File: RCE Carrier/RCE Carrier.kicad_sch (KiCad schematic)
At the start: 2 parts, among them J5 DF40C-34DP-0.4V_58_, J7 DF40C-34DP-0.4V_58_

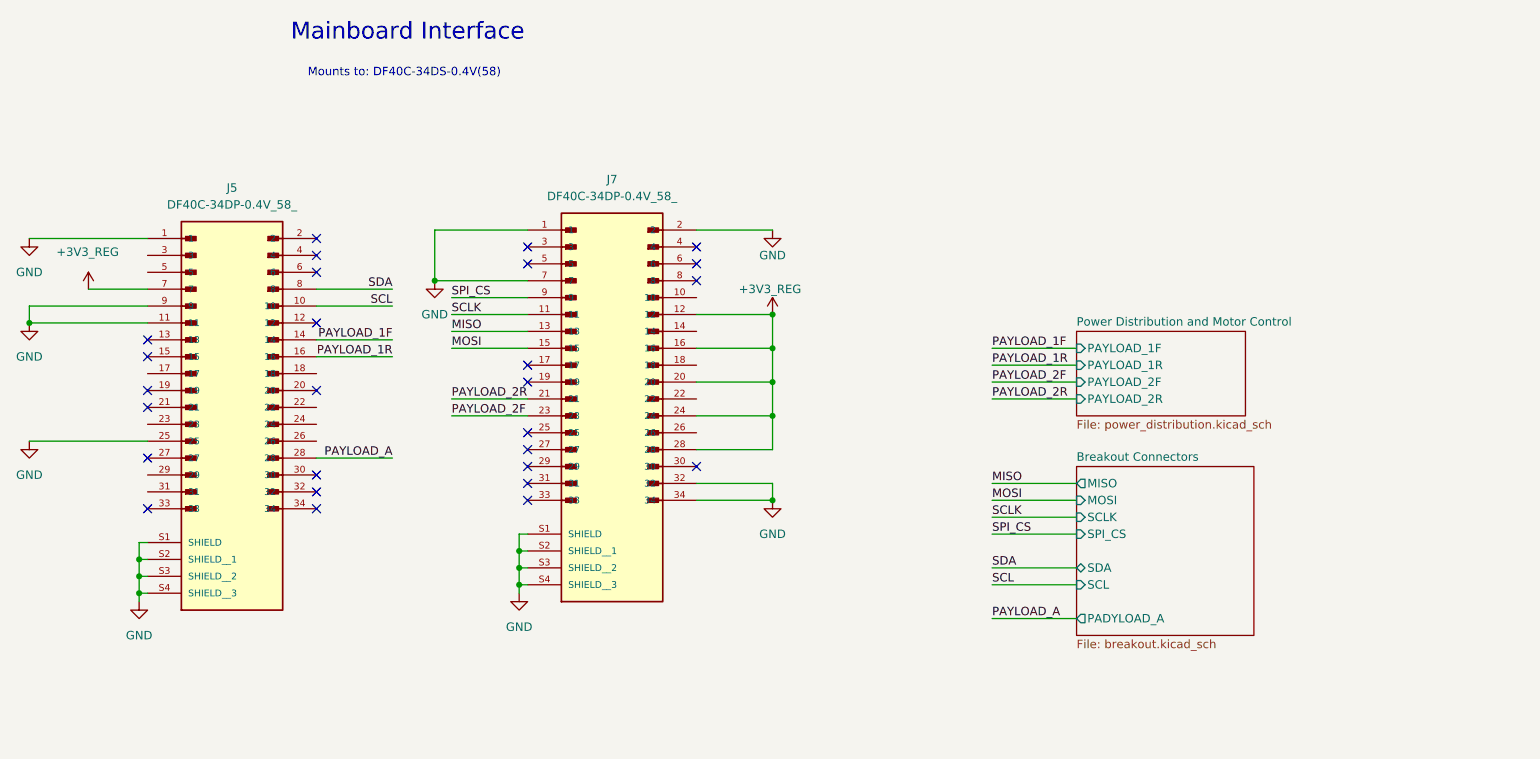
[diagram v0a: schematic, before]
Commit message: split pce and rce functions into two carriers, initial rce parts placement
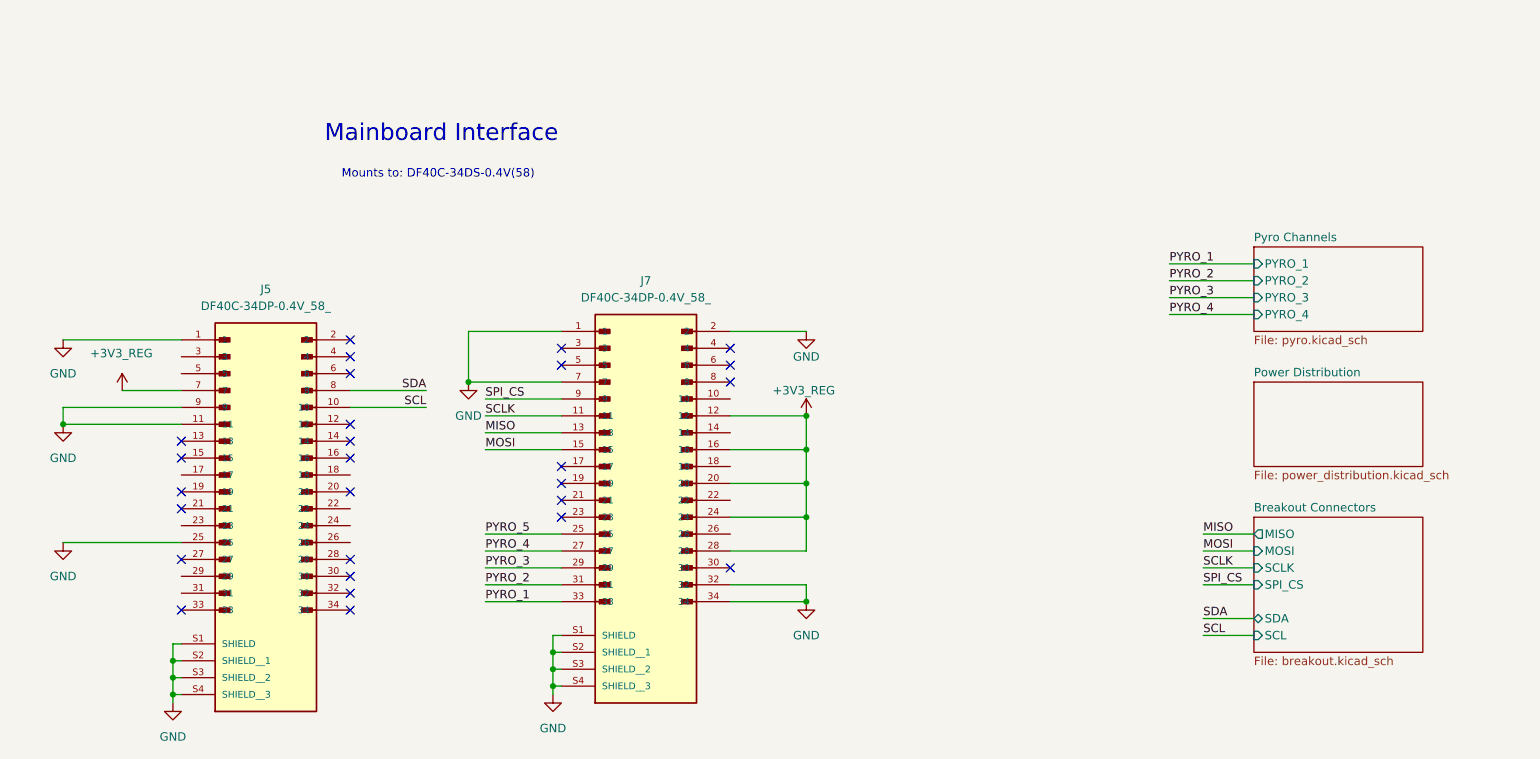
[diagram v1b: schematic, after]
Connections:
- net PYRO_5: now reaches J7.25
- net PYRO_4: now reaches J7.27
- net PYRO_3: now reaches J7.29
- net PYRO_2: now reaches J7.31
- net PYRO_1: now reaches J7.33
- net PAYLOAD_1F: no longer names the net of J5.14
- net PAYLOAD_1R: no longer names the net of J5.16
- net PAYLOAD_2F: no longer names the net of J7.23
- net PAYLOAD_2R: no longer names the net of J7.21
- net PAYLOAD_A: no longer names the net of J5.28
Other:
- removed sheet Power Distribution and Motor Control
- added sheet Power Distribution (power_distribution.kicad_sch)
- added sheet Pyro Channels (pyro.kicad_sch)
- sheet Breakout Connectors ports: added none; removed PADYLOAD_A
- title: Airdahl Flight Computer PCE Carrier Board -> Airdahl Flight Computer RCE Carrier Board

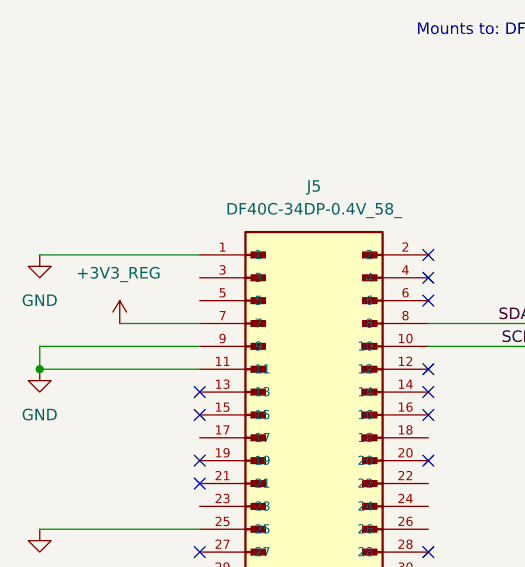
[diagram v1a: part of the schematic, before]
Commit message: added payload solenoid gpio, 3v3 rail from power mux to carriers, finished wiring
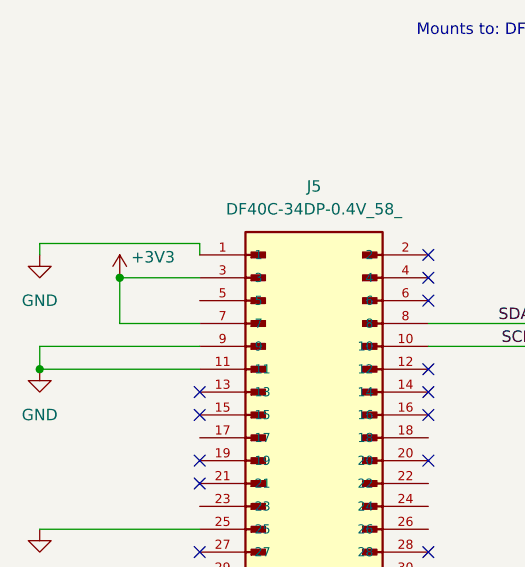
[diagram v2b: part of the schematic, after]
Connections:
- net +3V3_REG: no longer J5.7
- net +3V3: now reaches J5.3
- net +3V3: now also J5.7
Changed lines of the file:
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@@
+	)
+	(junction
+		(at 44.45 113.03)
+		(diameter 0)
+		(color 0 0 0 0)
 	)
 	(junction
@@
 	(wire
 		(pts
+			(xy 44.45 118.11) (xy 53.34 118.11)
+		)
+		(stroke
+			(width 0)
+			(type default)
+		)
+	)
+	(wire
+		(pts
 			(xy 99.06 119.38) (xy 110.49 119.38)
 		)
@@
 	(wire
 		(pts
+			(xy 53.34 109.22) (xy 53.34 110.49)
+		)
+		(stroke
+			(width 0)
+			(type default)
+		)
+	)
+	(wire
+		(pts
 			(xy 135.89 121.92) (xy 147.32 121.92)
 		)
@@
 	(wire
 		(pts
-			(xy 35.56 110.49) (xy 53.34 110.49)
+			(xy 35.56 109.22) (xy 53.34 109.22)
 		)
 		(stroke
@@
 	(wire
 		(pts
+			(xy 35.56 109.22) (xy 35.56 110.49)
+		)
+		(stroke
+			(width 0)
+			(type default)
+		)
+	)
+	(wire
+		(pts
+			(xy 44.45 113.03) (xy 53.34 113.03)
+		)
+		(stroke
+			(width 0)
+			(type default)
+		)
+	)
+	(wire
+		(pts
 			(xy 201.93 106.68) (xy 214.63 106.68)
 		)
@@
 	(wire
 		(pts
-			(xy 44.45 118.11) (xy 53.34 118.11)
-		)
-		(stroke
-			(width 0)
-			(type default)
-		)
-	)
-	(wire
-		(pts
 			(xy 52.07 165.1) (xy 52.07 163.83)
 		)
@@
 		(pts
 			(xy 78.74 118.11) (xy 90.17 118.11)
+		)
+		(stroke
+			(width 0)
+			(type default)
+		)
+	)
+	(wire
+		(pts
+			(xy 44.45 113.03) (xy 44.45 118.11)
 		)
 		(stroke
@@
 	(symbol
 		(lib_id "power:+3.3V")
-		(at 44.45 118.11 0)
+		(at 44.45 113.03 0)
 		(unit 1)
 		(body_style 1)
@@
 		(dnp no)
 		(property "Reference" "#PWR069"
-			(at 44.45 121.92 0)
-			(hide yes)
-			(show_name no)
-			(do_not_autoplace no)
-			(effects
-				(font
-					(size 1.27 1.27)
-				)
-			)
-		)
-		(property "Value" "+3V3_REG"
-			(at 39.624 112.522 0)
+			(at 44.45 116.84 0)
+			(hide yes)
+			(show_name no)
+			(do_not_autoplace no)
+			(effects
+				(font
+					(size 1.27 1.27)
+				)
+			)
+		)
+		(property "Value" "+3V3"
+			(at 45.72 110.744 0)
 			(show_name no)
 			(do_not_autoplace no)
@@
 		)
 		(property "Footprint" ""
-			(at 44.45 118.11 0)
+			(at 44.45 113.03 0)
 			(hide yes)
 			(show_name no)
@@
 		)
 		(property "Datasheet" ""
-			(at 44.45 118.11 0)
+			(at 44.45 113.03 0)
 			(hide yes)
 			(show_name no)
@@
 		)
 		(property "Description" "Power symbol creates a global label with name \"+3.3V\""
-			(at 44.45 118.11 0)
-			(hide yes)
-			(show_name no)
+			(at 44.45 113.03 0)
+			(hide yes)
+			(show_name no)
